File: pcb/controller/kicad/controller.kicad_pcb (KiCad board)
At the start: 4 copper layers, 70 x 110 mm, 99 parts, among them J1 43650-0300, J2 43045-0200, J3 43045-0600, J4 USB4105-GF-A, Q1 AO3400A, SW1 B3F-1002-G, SW2 B3F-1002-G, SW3 B3F-1002-G, U1 ESP32-C6-WROOM-1-N8, U10 TPS259470ARPWR, U11 ESDS312DBVR, U2 AP63203WU-7, U3 TCA9517ADGKR, U4 TPS3808G01DBVR, U5 TPS2553DBVR, U6 SN74LVC1G08DBVR, U7 SN74LVC1G14DBVR, U8 FSUSB42MUX, U9 USBLC6-2SC6

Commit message: Prepare simplified shared-power boards for routing
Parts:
- removed C22: 22uF, CrystalShim_Controller:Controller_C22
- removed C23: 4.7nF, CrystalShim_Controller:Controller_C23
- removed D5: SMBJ8.0CA, CrystalShim_Controller:Controller_D5
- removed D6: STPS2L40U, CrystalShim_Controller:Controller_D6
- removed R30: 26.1kΩ, CrystalShim_Controller:Controller_R30
- removed R31: 10kΩ, CrystalShim_Controller:Controller_R31
- removed R32: 470kΩ, CrystalShim_Controller:Controller_R32
- removed R33: 38.3kΩ, CrystalShim_Controller:Controller_R33
- removed R34: 10kΩ, CrystalShim_Controller:Controller_R34
- removed R35: 470kΩ, CrystalShim_Controller:Controller_R35
- removed R36: 2.87kΩ, CrystalShim_Controller:Controller_R36
- removed R37: 2.2kΩ, CrystalShim_Controller:Controller_R37
- removed U10: TPS259470ARPWR, CrystalShim_Controller:Controller_U10
- added C45: 100nF, CrystalShim_Controller:Controller_C45, F.Cu at (50.5, 79.0)
- added C46: 100nF, CrystalShim_Controller:Controller_C46, F.Cu at (61.5, 79.0)
- added C47: 22uF, CrystalShim_Controller:Controller_C47, F.Cu at (57.0, 131.0)
- added D10: STPS2L40U, CrystalShim_Controller:Controller_D10, F.Cu at (136.0, 111.0)
- added D11: STPS2L40U, CrystalShim_Controller:Controller_D11, F.Cu at (136.0, 93.0)
- added D8: SMBJ7.0A, CrystalShim_Controller:Controller_D8, F.Cu at (48.5, 67.0)
- added D9: STPS2L40U, CrystalShim_Controller:Controller_D9, F.Cu at (136.0, 129.0)
- added J5: 43045-0600, CrystalShim_Controller:Controller_J5, F.Cu at (56.0, 59.0)
- added J6: 43045-0200, CrystalShim_Controller:Controller_J6, F.Cu at (56.0, 141.0)
- added J7: 43045-0200, CrystalShim_Controller:Controller_J7, F.Cu at (144.0, 135.0)
- added J8: 43045-0200, CrystalShim_Controller:Controller_J8, F.Cu at (144.0, 117.0)
- added J9: 43045-0200, CrystalShim_Controller:Controller_J9, F.Cu at (144.0, 99.0)
- added Q2: AO3400A, CrystalShim_Controller:Controller_Q2, F.Cu at (135.0, 135.0)
- added Q3: AO3400A, CrystalShim_Controller:Controller_Q3, F.Cu at (135.0, 117.0)
- added Q4: AO3400A, CrystalShim_Controller:Controller_Q4, F.Cu at (135.0, 99.0)
- added R69: 6.8Ω, CrystalShim_Controller:Controller_R69, F.Cu at (56.0, 89.0)
- added R70: 22Ω, CrystalShim_Controller:Controller_R70, F.Cu at (54.5, 72.0)
- added R71: 22Ω, CrystalShim_Controller:Controller_R71, F.Cu at (58.0, 72.0)
- added R72: 2.7kΩ, CrystalShim_Controller:Controller_R72, F.Cu at (54.0, 83.0)
- added R73: 2.7kΩ, CrystalShim_Controller:Controller_R73, F.Cu at (57.5, 83.0)
- added R80: 100Ω, CrystalShim_Controller:Controller_R80, F.Cu at (134.0, 139.0)
- added R81: 10kΩ, CrystalShim_Controller:Controller_R81, F.Cu at (134.0, 142.0)
- added R82: 100Ω, CrystalShim_Controller:Controller_R82, F.Cu at (134.0, 121.0)
- added R83: 10kΩ, CrystalShim_Controller:Controller_R83, F.Cu at (134.0, 124.0)
- added R84: 100Ω, CrystalShim_Controller:Controller_R84, F.Cu at (134.0, 103.0)
- added R85: 10kΩ, CrystalShim_Controller:Controller_R85, F.Cu at (134.0, 106.0)
- added TP12: TP12, CrystalShim_Controller:Controller_TP12, F.Cu at (90.0, 149.0)
- added TP13: TP13, CrystalShim_Controller:Controller_TP13, F.Cu at (98.0, 149.0)
- added TP14: TP14, CrystalShim_Controller:Controller_TP14, F.Cu at (98.0, 141.0)
- added U12: TCA9517ADGKR, CrystalShim_Controller:Controller_U12, F.Cu at (56.0, 78.0)
- added U13: ESDS312DBVR, CrystalShim_Controller:Controller_U13, F.Cu at (56.0, 67.0)
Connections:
- C20 pad 1: V5_SERVICE_RAW -> V5_SERVICE
- C21 pad 1: V5_SERVICE_RAW -> V5_SERVICE
- J2 pad 1: V5_SERVICE_RAW -> V5_SERVICE
- J4 pad A8: (no net) -> unconnected-(J4-PadA8)
- J4 pad B8: (no net) -> unconnected-(J4-PadB8)
- U1 pad 22: (no net) -> unconnected-(U1-NC-Pad22)
- U1 pad 23: (no net) -> unconnected-(U1-IO15-Pad23)
- U1 pad 26: (no net) -> PUMP_DECHLOR
- U1 pad 27: (no net) -> PUMP_CHLORINE
- U1 pad 4: (no net) -> ACCESSORY_INPUT1
- U1 pad 5: (no net) -> ACCESSORY_INPUT2
- U1 pad 6: (no net) -> RESERVOIR_SDA
- U1 pad 7: (no net) -> RESERVOIR_SCL
- U1 pad 9: (no net) -> PUMP_TRANSFER
- U11 pad 1: (no net) -> unconnected-(U11-NC_1-Pad1)
- U11 pad 3: (no net) -> unconnected-(U11-NC_3-Pad3)
- U4 pad 4: (no net) -> unconnected-(U4-CT-Pad4)
- U7 pad 1: (no net) -> unconnected-(U7-NC-Pad1)
- U8 pad 8: (no net) -> unconnected-(U8-HSD2_N-Pad8)
- U8 pad 9: (no net) -> unconnected-(U8-HSD2_P-Pad9)
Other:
- board size 70 x 110 mm -> 110 x 110 mm

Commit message: Prepare filled planes and enforce KiCad routing guardrails
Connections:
- net USB_D_N_PORT renamed USB_D_PORT_N
- net USB_D_N_SWITCH renamed USB_D_SWITCH_N
- net USB_D_P_PORT renamed USB_D_PORT_P
- net USB_D_P_SWITCH renamed USB_D_SWITCH_P
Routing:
- net GND: vias 0 -> 25
- added copper zone on B.Cu, net GND
- added copper zone on F.Cu, net GND
- added copper zone on In1.Cu, net GND

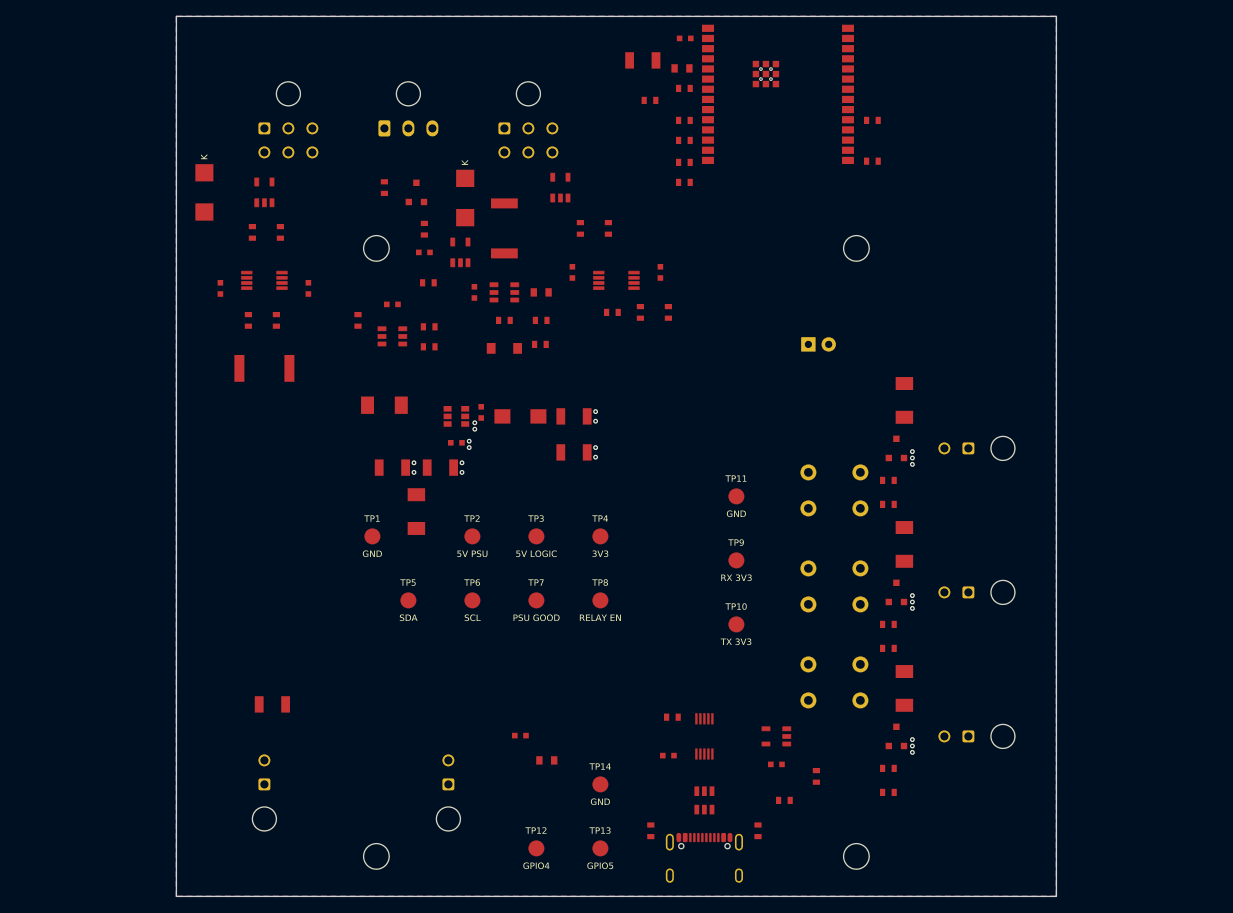
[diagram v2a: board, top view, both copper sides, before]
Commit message: Prepare compact three-board designs for owner routing
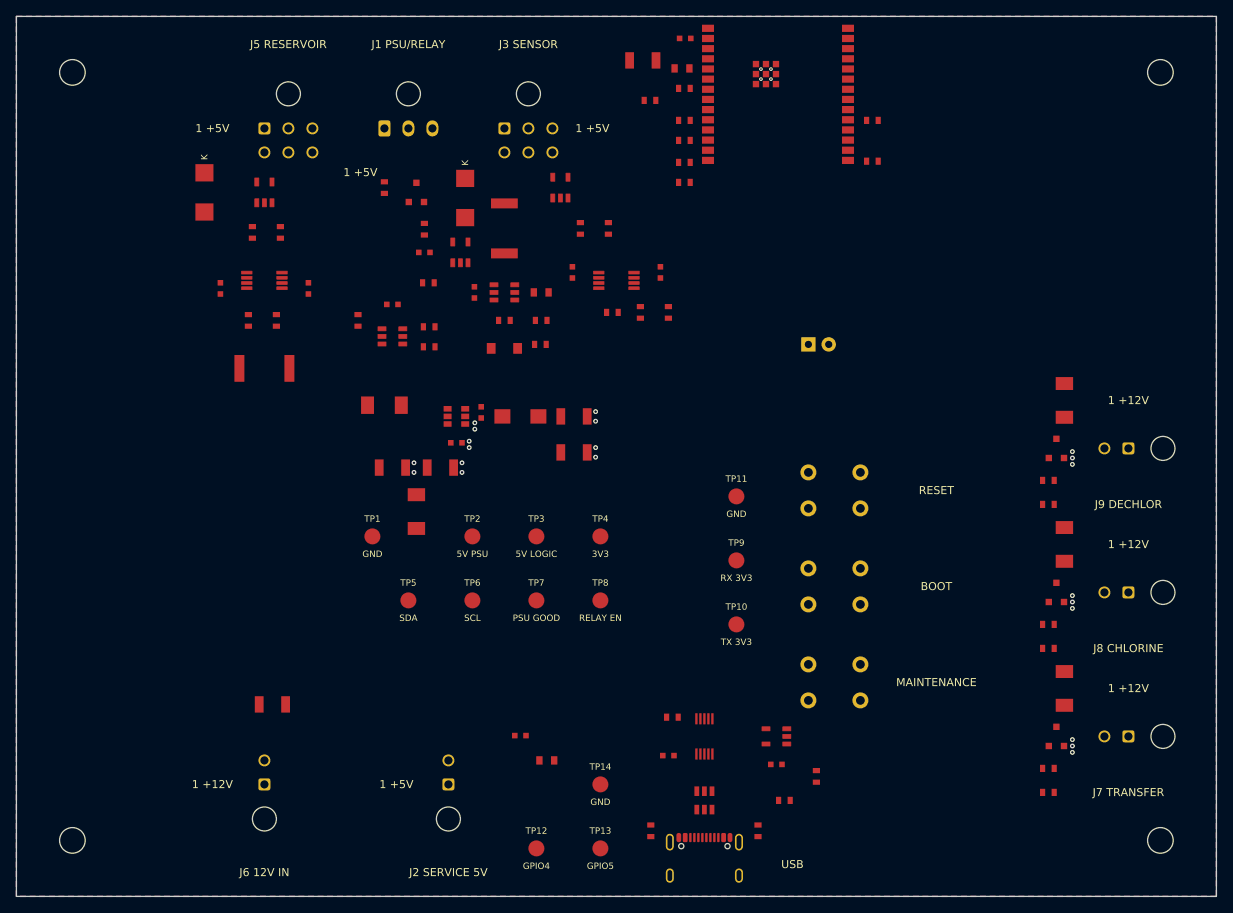
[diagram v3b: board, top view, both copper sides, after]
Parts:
- moved H1 43.9 mm to (32.0, 52.0)
- moved H2 43.9 mm to (168.0, 52.0)
- moved H3 38.1 mm to (32.0, 148.0)
- moved H4 38.1 mm to (168.0, 148.0)
- moved D10 20.0 mm to (156.0, 111.0)
- moved D11 20.0 mm to (156.0, 93.0)
- moved D9 20.0 mm to (156.0, 129.0)
- moved J7 20.0 mm to (164.0, 135.0)
- moved J8 20.0 mm to (164.0, 117.0)
- moved J9 20.0 mm to (164.0, 99.0)
- moved Q2 20.0 mm to (155.0, 135.0)
- moved Q3 20.0 mm to (155.0, 117.0)
- moved Q4 20.0 mm to (155.0, 99.0)
- moved R80 20.0 mm to (154.0, 139.0)
- moved R81 20.0 mm to (154.0, 142.0)
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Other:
- board size 110 x 110 mm -> 150 x 110 mm
- board text added: "1 +12V"
- board text added: "1 +5V"
- board text added: "BOOT"
- board text added: "FABRICATION REQUIREMENTS JLC04161H-7628 / nominal 1.6 mm / ENIG / green mask USB differential impedance acceptance: 81-99 ohm Stencil: 0.100 mm laser cut; J4 shells hand soldered U1 ground vias: top and bottom tented, no extra apertures Native 0.010 mm mask and Df 0.02 are visualization defaults only. Do not use native/Gerber-job default stack metadata as order constraints. Use reviewed vendor st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"
- board text added: "J1 PSU/RELAY"
- board text added: "J2 SERVICE 5V"
- board text added: "J3 SENSOR"
- board text added: "J5 RESERVOIR"
- board text added: "J6 12V IN"
- board text added: "J7 TRANSFER"
- board text added: "J8 CHLORINE"
- board text added: "J9 DECHLOR"
- board text added: "MAINTENANCE"
- board text added: "RESET"
- board text added: "USB"

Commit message: Simplify mains connectors and separate the 5 V service input
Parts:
- J2: value 43045-0200 -> S2B-XH-A
- turned J2 to 0 degrees
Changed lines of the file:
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@@
 	(footprint "CrystalShim_Controller:Controller_J2"
 		(layer "F.Cu")
-		(at 79 141 180)
+		(at 79 141)
 		(property "Reference" "J2"
-			(at 0 -3 0)
+			(at 0 -3 180)
 			(layer "F.SilkS")
 			(hide yes)
@@
 			)
 		)
-		(property "Value" "43045-0200"
-			(at 0 3 0)
+		(property "Value" "S2B-XH-A"
+			(at 0 3 180)
 			(layer "F.Fab")
 			(hide yes)
@@
 			)
 		)
-		(property "Datasheet" "https://www.molex.com/content/dam/molex/molex-dot-com/products/automated/en-us/salesdrawingpdf/430/43045/430450200_sd.pdf"
-			(at 0 0 0)
+		(property "Datasheet" "https://www.jst.com/wp-content/uploads/2025/06/eXH.pdf"
+			(at 0 0 180)
 			(layer "F.Fab")
 			(hide yes)
@@
 		)
 		(property "Description" "Integrated Circuit"
-			(at 0 0 0)
+			(at 0 0 180)
 			(layer "F.Fab")
 			(hide yes)
@@
 		)
 		(property "Supplier Part Number" ""
-			(at 0 0 0)
+			(at 0 0 180)
 			(layer "F.Fab")
 			(hide yes)
@@
 			)
 		)
-		(property "MPN" "43045-0200"
-			(at 0 0 0)
+		(property "MPN" "S2B-XH-A"
+			(at 0 0 180)
 			(layer "F.SilkS")
 			(hide yes)
@@
 		)
 		(duplicate_pad_numbers_are_jumpers no)
-		(fp_poly
-			(pts
-				(xy -4.45 -9.75) (xy 4.45 -9.75) (xy 4.45 4.4) (xy -4.45 4.4) (xy -4.45 -9.75)
+		(fp_line
+			(start -3.45 -3.3)
+			(end 5.95 -3.3)
+			(stroke
+				(width 0.05)
+				(type default)
 			)
+			(layer "F.CrtYd")
+		)
+		(fp_line
+			(start -3.45 10.2)
+			(end -3.45 -3.3)
 			(stroke
 				(width 0.05)
 				(type default)
 			)
-			(fill no)
 			(layer "F.CrtYd")
 		)
 		(fp_line
-			(start 3.575 0.99)
-			(end -3.575 0.99)
+			(start 5.95 -3.3)
+			(end 5.95 10.2)
+			(stroke
+				(width 0.05)
+				(type default)
+			)
+			(layer "F.CrtYd")
+		)
+		(fp_line
+			(start 5.95 10.2)
+			(end -3.45 10.2)
+			(stroke
+				(width 0.05)
+				(type default)
+			)
+			(layer "F.CrtYd")
+		)
+		(fp_line
+			(start -2.45 -2.3)
+			(end 4.95 -2.3)
 			(stroke
 				(width 0.1)
@@
 		)
 		(fp_line
-			(start 3.575 -8.92)
-			(end 3.575 0.99)
+			(start -2.45 9.2)
+			(end -2.45 -2.3)
 			(stroke
 				(width 0.1)
@@
 		)
 		(fp_line
-			(start -3.575 0.99)
-			(end -3.575 -8.92)
+			(start 4.95 -2.3)
+			(end 4.95 9.2)
 			(stroke
 				(width 0.1)
@@
 		)
 		(fp_line
-			(start -3.575 -8.92)
-			(end 3.575 -8.92)
+			(start 4.95 9.2)
+			(end -2.45 9.2)
 			(stroke
 				(width 0.1)
@@
 			(layer "F.Fab")
 		)
-		(pad "" np_thru_hole circle
-			(at 0 -4.32)
-			(size 3 3)
-			(drill 3)
-			(layers "*.Cu" "*.Mask")
-		)
 		(pad "1" thru_hole roundrect
-			(at 0 0 180)
-			(size 1.5 1.5)
-			(drill 1.02)
+			(at 0 0)
+			(size 1.7 2)
+			(drill 1)
 			(layers "*.Cu" "*.Mask")
 			(remove_unused_layers no)
-			(roundrect_rratio 0.1666666667)
+			(roundrect_rratio 0.1470588235)
 			(net "V5_SERVICE")
 			(solder_mask_margin 0.05)
 		)
-		(pad "2" thru_hole circle
-			(at 0 3)
-			(size 1.5 1.5)
-			(drill 1.02)
+		(pad "2" thru_hole oval
+			(at 2.5 0)
+			(size 1.7 2)
+			(drill 1)
 			(layers "*.Cu" "*.Mask")
 			(remove_unused_layers no)
 			(net "GND")
 			(solder_mask_margin 0.05)
+			(thermal_bridge_angle 45)
 		)
 		(embedded_fonts no)
@@
 		(polygon
 			(pts
-				(xy 77.25 139.25) (xy 80.75 139.25) (xy 80.75 142.75) (xy 77.25 142.75)
+				(xy 77.15 139) (xy 80.85 139) (xy 80.85 143) (xy 77.15 143)
 			)
 		)

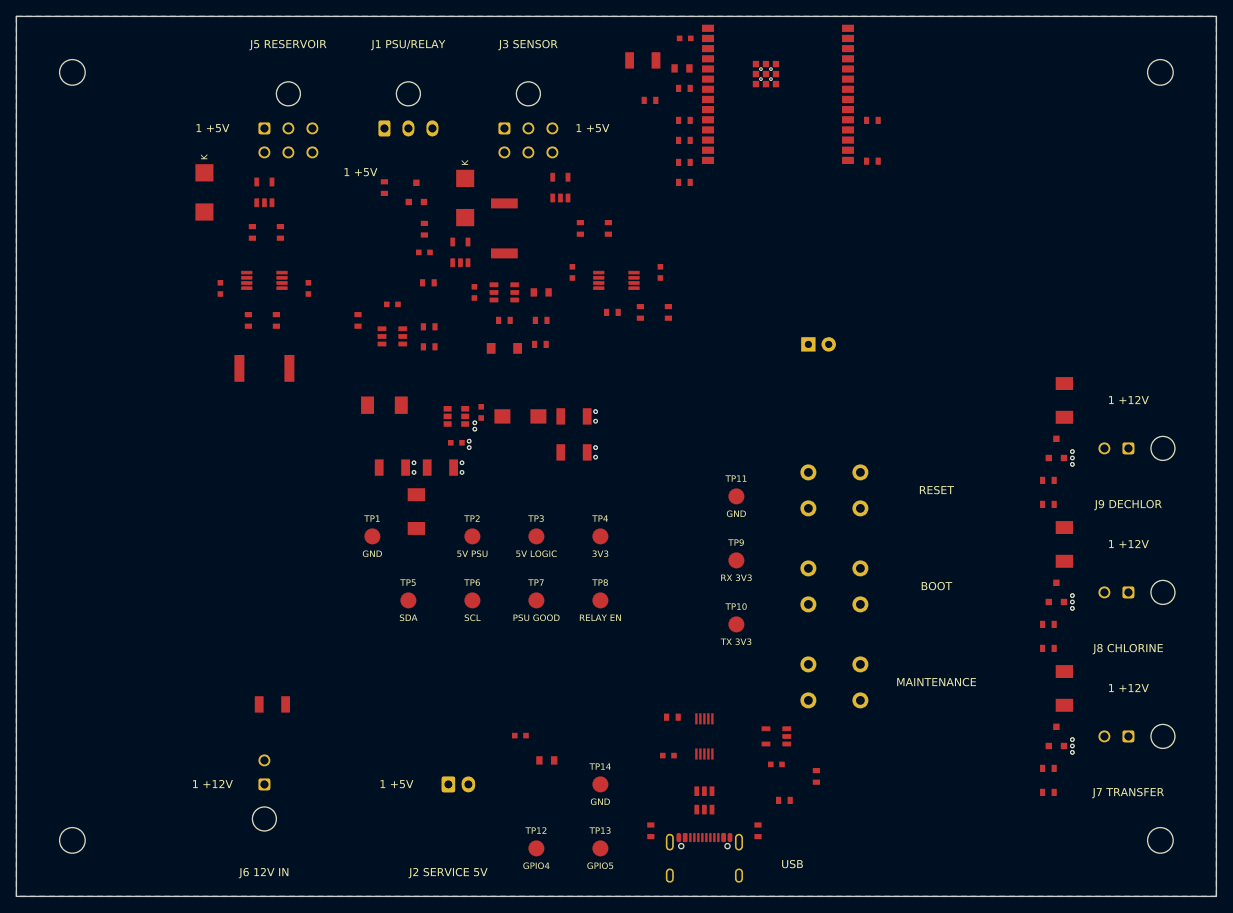
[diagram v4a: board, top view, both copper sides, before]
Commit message: Prepare all three boards for standard JLCPCB ordering
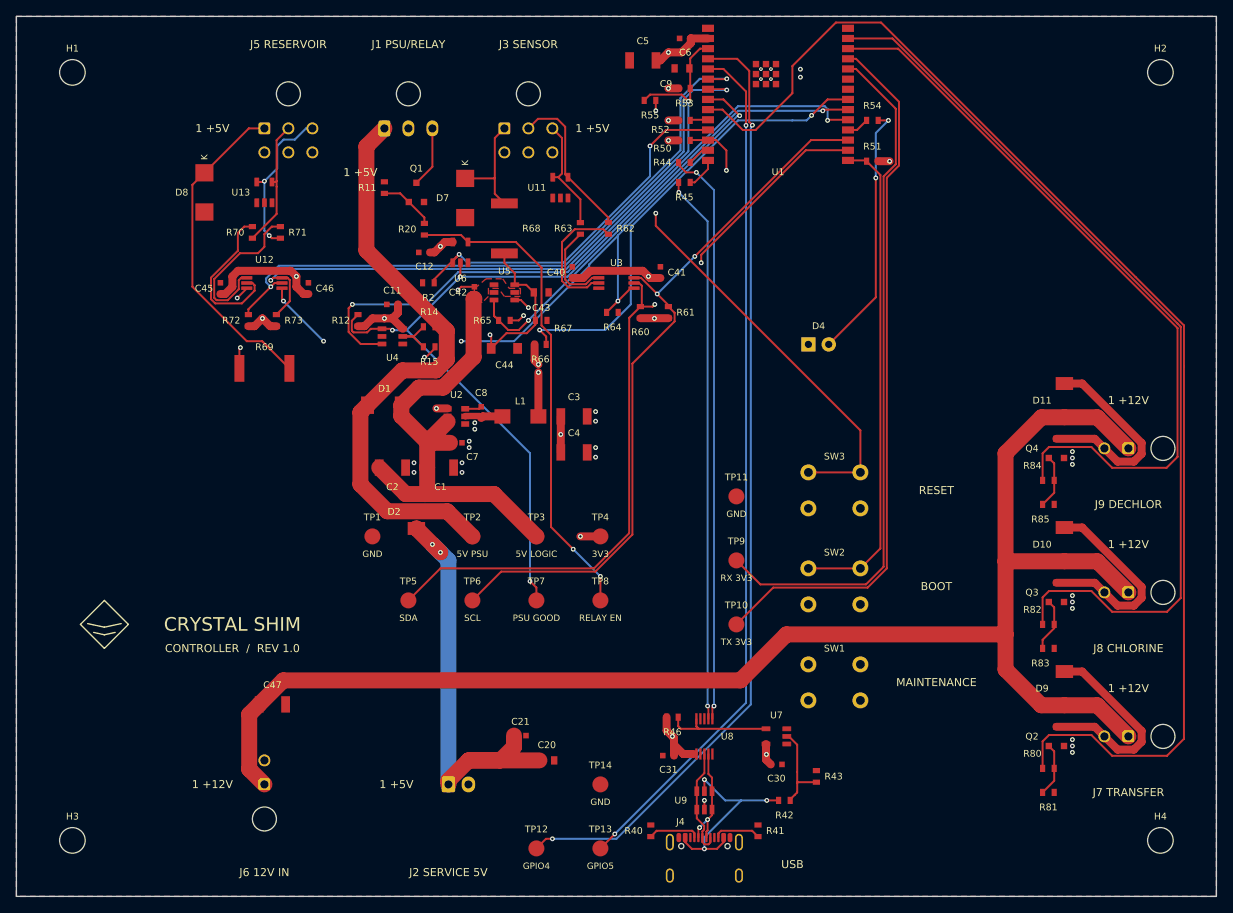
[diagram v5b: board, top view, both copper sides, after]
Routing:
- net V3V3: track 0.00 -> 324.9 mm, vias 0 -> 18
- net V12_PUMP: track 0.00 -> 189.9 mm
- net PUMP_TRANSFER: track 0.00 -> 158.8 mm
- net PSU_GOOD: track 0.00 -> 120.6 mm, vias 0 -> 4
- net ACCESSORY_INPUT1: track 0.00 -> 119.5 mm, vias 0 -> 2
- net PUMP_CHLORINE: track 0.00 -> 113.2 mm
- net ACCESSORY_INPUT2: track 0.00 -> 108.1 mm, vias 0 -> 2
- net SENSOR_SDA: track 0.00 -> 98.4 mm, vias 0 -> 2
- net PUMP_DECHLOR: track 0.00 -> 94.0 mm
- net SENSOR_SCL: track 0.00 -> 92.1 mm, vias 0 -> 2
- net SENSOR_BUS_EN: track 0.00 -> 90.3 mm, vias 0 -> 5
- net UART0_TX: track 0.00 -> 89.3 mm
- net UART0_RX: track 0.00 -> 86.5 mm
- net RESERVOIR_SDA: track 0.00 -> 81.6 mm, vias 0 -> 2
- net RESERVOIR_SCL: track 0.00 -> 80.7 mm, vias 0 -> 2
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- added copper zone on F.Cu, net V5_LOGIC
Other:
- board text added: "CONTROLLER / REV 1.0"
- board text added: "CRYSTAL SHIM"
- board text added: "CRYSTAL SHIM CONTROLLER 4 layers / nominal 1.6 mm / ENIG Standard JLCPCB No requirement stack No impedance control / No PCB assembly Tented vias; no filling, capping or plugging CAD mask and dielectric-loss defaults are nonbinding."
- board text removed: "FABRICATION REQUIREMENTS JLC04161H-7628 / nominal 1.6 mm / ENIG / green mask USB differential impedance acceptance: 81-99 ohm Stencil: 0.100 mm laser cut; J4 shells hand soldered U1 ground vias: top and bottom tented, no extra apertures Native 0.010 mm mask and Df 0.02 are visualization defaults only. Do not use native/Gerber-job default stack metadata as order constraints. Use reviewed vendor st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"
